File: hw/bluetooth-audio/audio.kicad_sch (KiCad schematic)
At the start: 39 parts, among them J1 AudioJack4_Ground, U4 ES8388

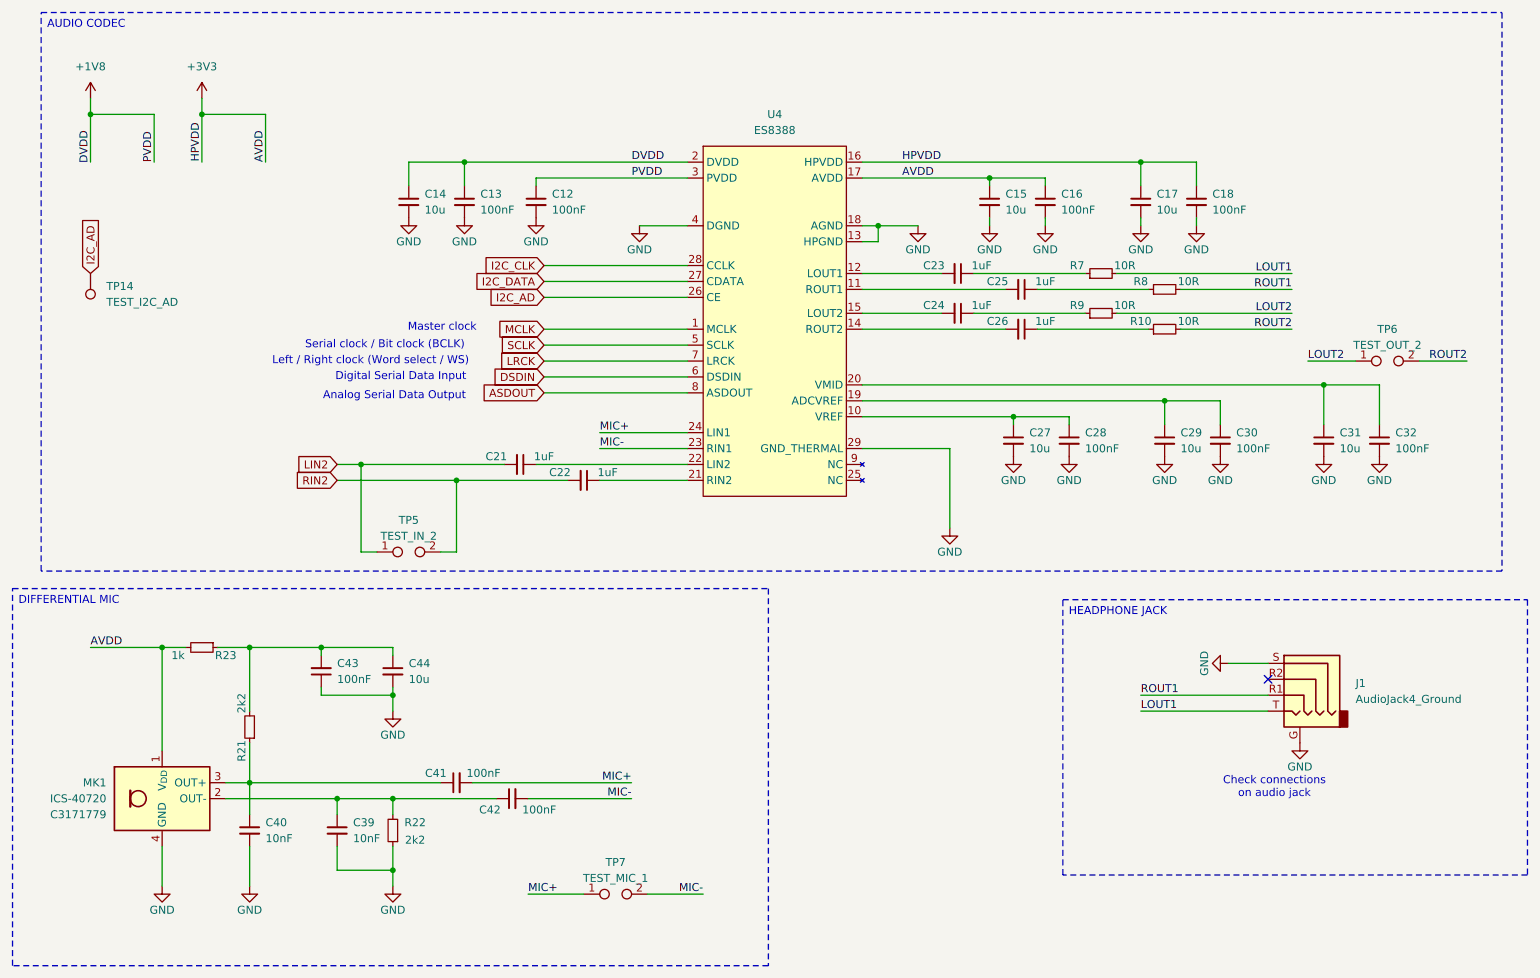
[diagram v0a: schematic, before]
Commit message: Custom symbol and footprints for IS2083. Updated design document. Initial dump of components onto cleared PCB.
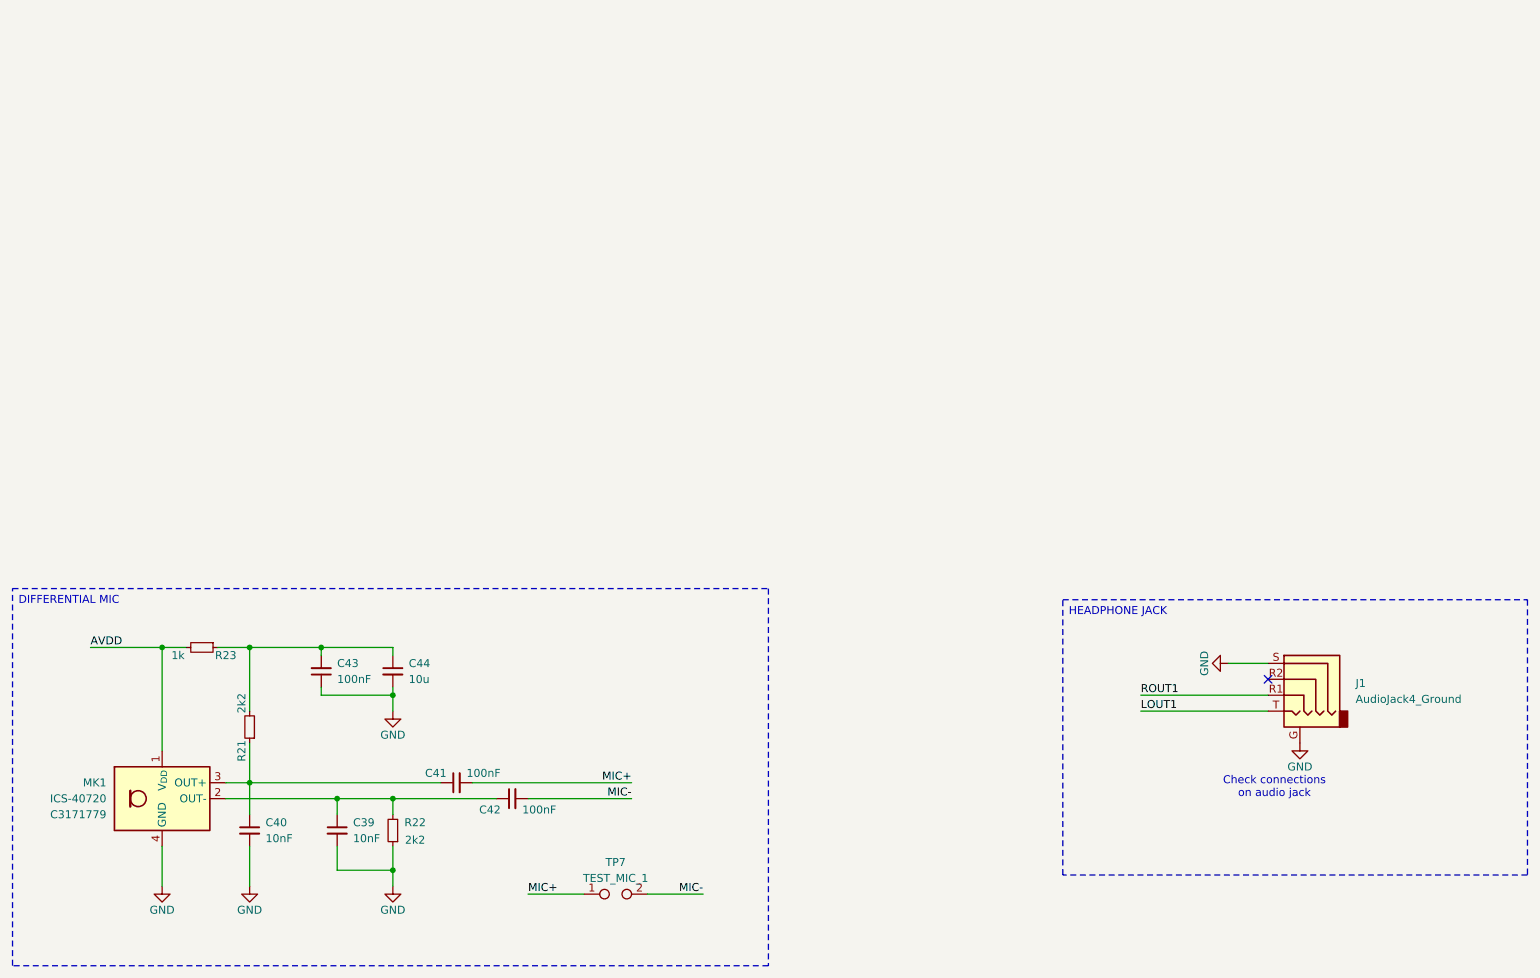
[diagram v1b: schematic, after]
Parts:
- removed C12, C13, C16, C18, C28, C30, C32: 100nF, Capacitor_SMD:C_0402_1005Metric, symbol Device:C_Small
- removed C14, C15, C17, C29, C31: 10u, Capacitor_SMD:C_0603_1608Metric, symbol Device:C_Small
- removed C21, C22, C23, C24, C25, C26: 1uF, Capacitor_SMD:C_0402_1005Metric, symbol Device:C_Small
- removed C27: 10u, Capacitor_SMD:C_0402_1005Metric, symbol Device:C_Small
- removed R10, R7, R8, R9: 10R, Resistor_SMD:R_0402_1005Metric, symbol Device:R_Small
- removed TP14: TEST_I2C_AD, TestPoint:TestPoint_Pad_D1.0mm, symbol Connector:TestPoint
- removed TP5: TEST_IN_2, custom_footprints:TestPoint_Pad_2x1_D1.0mm, symbol Connector:TestPoint_2Pole
- removed TP6: TEST_OUT_2, custom_footprints:TestPoint_Pad_2x1_D1.0mm, symbol Connector:TestPoint_2Pole
- removed U4: ES8388, Package_DFN_QFN:QFN-28-1EP_4x4mm_P0.4mm_EP2.3x2.3mm, symbol custom_symbols:ES8388
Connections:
- net +3V3 renamed AVDD
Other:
- note removed: "Analog Serial Data Output"
- note removed: "Digital Serial Data Input"
- note removed: "Left / Right clock (Word select / WS)"
- note removed: "Master clock"
- note removed: "Serial clock / Bit clock (BCLK)"

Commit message: All decoupling caps and labels on IS2083
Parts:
- removed C39, C40: 10nF, Capacitor_SMD:C_0402_1005Metric, symbol Device:C_Small
- removed C41, C42, C43: 100nF, Capacitor_SMD:C_0402_1005Metric, symbol Device:C_Small
- removed C44: 10u, Capacitor_SMD:C_0603_1608Metric, symbol Device:C_Small
- removed J1: AudioJack4_Ground, Connector_Audio:Jack_3.5mm_KoreanHropartsElec_PJ-320D-4A_Horizontal, symbol Connector_Audio:AudioJack4_Ground
- removed MK1: ICS-40720, custom_footprints:ICS40720, symbol custom_symbols:ICS-40720
- removed R21, R22: 2k2, Resistor_SMD:R_0402_1005Metric, symbol Device:R_Small
- removed R23: 1k, Resistor_SMD:R_0402_1005Metric, symbol Device:R_Small
- removed TP7: TEST_MIC_1, custom_footprints:TestPoint_Pad_2x1_D1.0mm, symbol Connector:TestPoint_2Pole
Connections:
- no-connect marks 1 -> 0
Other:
- note removed: "Check connections on audio jack"

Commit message: Fixing sheet titles
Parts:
- added C45, C49: 10nF, Capacitor_SMD:C_0402_1005Metric, symbol Device:C_Small
- added C47, C51, C52: 100nF, Capacitor_SMD:C_0402_1005Metric, symbol Device:C_Small
- added C50: 10u, Capacitor_SMD:C_0603_1608Metric, symbol Device:C_Small
- added J3: AudioJack4_Ground, Connector_Audio:Jack_3.5mm_KoreanHropartsElec_PJ-320D-4A_Horizontal, symbol Connector_Audio:AudioJack4_Ground
- added MK2: ICS-40720, custom_footprints:ICS40720, symbol custom_symbols:ICS-40720
- added R24: 1k, Resistor_SMD:R_0402_1005Metric, symbol Device:R_Small
- added R25, R26: 2k2, Resistor_SMD:R_0402_1005Metric, symbol Device:R_Small
- added TP8: TEST_MIC_1, custom_footprints:TestPoint_Pad_2x1_D1.0mm, symbol Connector:TestPoint_2Pole
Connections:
- new net: C45.1, C51.1, MK2.3 (OUT+), R25.1
- new net: C47.2, C50.1, R24.1, R25.2
- new net: C49.1, C52.1, MK2.2 (OUT-), R26.2
- new net AVDD: MK2.1 (V_{DD}), R24.2
- new net GND: C45.2, C47.1, C49.2, C50.2, J3.G, J3.S, MK2.4 (GND), R26.1
- new net LOUT1: J3.T
- new net MIC+: C51.2, TP8.1
- new net MIC-: C52.2, TP8.2
- new net ROUT1: J3.R1
- no-connect marks 0 -> 1
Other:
- note added: "Check connections on audio jack"
